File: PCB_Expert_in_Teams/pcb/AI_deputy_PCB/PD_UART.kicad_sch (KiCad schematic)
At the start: 1 part, among them J2 Battery Input

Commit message: updating repo from desktop
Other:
- company: (none) -> Area 42 & Albers-Online Psykologi
- title: (none) -> AI Deputy
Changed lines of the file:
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@@
 	(generator_version "9.0")
 	(paper "A4")
+	(title_block
+		(title "AI Deputy")
+		(date "2025-09-24")
+		(rev "v0.1")
+		(company "Area 42 & Albers-Online Psykologi")
+		(comment 1 "SDU")
+		(comment 2 "Expert In Teams Semester Project")
+	)
 	(text_box "Battery input from BMS\n"
 		(exclude_from_sim no)

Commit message: 29/10/update
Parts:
- removed J2: Battery Input, symbol Connector:Conn_01x02_Pin
- added C38, C41, C45, C47, C48: 4u7, symbol Device:C
- added C39, C40, C42, C49: 100n, symbol Device:C
- added D3: LED, LED_SMD:LED_0805_2012Metric_Pad1.15x1.40mm_HandSolder, symbol Device:LED
- added IC7: CYPD3177-24LQXQ, QFN50P400X400X60-25N-D, symbol CYPD3177-24LQXQ:CYPD3177-24LQXQ
- added J16: USB_C_Receptacle_USB2.0_16P, EXT_AI_DEPUTY_Library:MOLEX_1054500101, symbol Connector:USB_C_Receptacle_USB2.0_16P
- added Q2, Q4: DMP3098LSD-13, SOIC127P600X175-8N, symbol DMP3098LSD:DMP3098LSD-13
- added R20, R22, R24: 5.1k, Resistor_SMD:R_0805_2012Metric_Pad1.20x1.40mm_HandSolder, symbol Device:R
- added R21, R25, R35: 1k, Resistor_SMD:R_0805_2012Metric_Pad1.20x1.40mm_HandSolder, symbol Device:R
- added R23: 2.4k, Resistor_SMD:R_0805_2012Metric_Pad1.20x1.40mm_HandSolder, symbol Device:R
- added R26: 2.2k, Resistor_SMD:R_0805_2012Metric_Pad1.20x1.40mm_HandSolder, symbol Device:R
- added R27, R28, R29, R31, R32: 2k2, symbol Device:R
- added R30: 20k, symbol Device:R
- added R33: 10k, Resistor_SMD:R_0805_2012Metric_Pad1.20x1.40mm_HandSolder, symbol Device:R
- added R34: 4.7k, Resistor_SMD:R_0805_2012Metric_Pad1.20x1.40mm_HandSolder, symbol Device:R
- added R36: 50k, Resistor_SMD:R_0805_2012Metric_Pad1.20x1.40mm_HandSolder, symbol Device:R
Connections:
- net GND: now also C38.2, C39.2, C40.2, C41.2, C42.2, C45.2, C48.2, D3.1 (K), IC7.19 (GND_1), IC7.22 (GND_2), IC7.25 (GND_3), J16.A1 (GND), J16.A12 (GND), J16.B1 (GND), J16.B12 (GND), R21.2, R23.2, R25.2, R26.2
- new net: C45.1, IC7.24 (VCCD)
- new net: C47.2, C49.2, R30.2, R31.2, R32.1
- new net: IC7.10 (FLIP), R34.2
- new net: IC7.1 (VBUS_MIN), R20.2, R21.1
- new net: IC7.5 (ISNK_COARSE), R22.2, R23.1
- new net: D3.2 (A), R33.2
- new net: Q4.1 (S1), Q4.3 (S2)
- new net: Q4.2 (G1), Q4.4 (G2), R31.1
- new net: IC7.2 (VBUS_MAX), R24.2, R25.1
- new net: IC7.6 (ISNK_FINE), R26.1
- new net: Q2.1 (S1), Q2.3 (S2)
- new net: Q2.2 (G1), Q2.4 (G2), R35.1, R36.2
- new net +3V3: C38.1, C39.1, C40.1, IC7.23 (VDDD), R20.1, R22.1, R24.1, R27.1, R28.1, R29.1, R34.1
- new net CC1: IC7.15 (CC1), J16.A5 (CC1)
- new net CC2: IC7.14 (CC2), J16.B5 (CC2)
- new net D+: J16.A6 (D+), J16.B6 (D+)
- new net D-: J16.A7 (D-), J16.B7 (D-)
- new net PD_Fault: IC7.9 (FAULT), R33.1
- new net PD_INT: IC7.7 (HPI_INT), R29.2
- new net SAFE_PWR_EN: IC7.4 (SAFE_PWR_EN), R35.2
- new net SCL: IC7.13 (HPI_SCL), R27.2
- new net SDA: IC7.12 (HPI_SDA), R28.2
- new net VBUS: C41.1, C42.1, C47.1, IC7.18 (VBUS_IN), J16.A4 (VBUS), J16.A9 (VBUS), J16.B4 (VBUS), J16.B9 (VBUS), Q2.7 (D1_1), Q2.8 (D1_2), Q4.7 (D1_1), Q4.8 (D1_2), R30.1, R36.1
- new net VBUSEN: IC7.3 (VBUS_FET_EN), R32.2
- new net VDC_OUT: C48.1, C49.1, IC7.11 (VDC_OUT), Q4.6 (D2_2)
- new net VIN: Q2.5 (D2_1), Q2.6 (D2_2)
- no-connect marks 0 -> 8
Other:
- note added: "1/6 for 9V (see datasheet for config)"
- note added: "Fuse or TVS?"
- note added: "USB-C 3.0 footprint?"
- note added: "VIN goes to input 3v3 step down converter"
- note added: "current config is 2A, 5.1k up and 5.1k down for 3A"
- note added: "find fitting res value for led"

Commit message: update some schematic footprints
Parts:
- IC7: footprint QFN50P400X400X60-25N-D -> EXT_AI_DEPUTY_Library:QFN50P400X400X60-25N-D
- Q2, Q4: footprint SOIC127P600X175-8N -> EXT_AI_DEPUTY_Library:SOIC127P600X175-8N
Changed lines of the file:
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@@
 			)
 		)
-		(property "Footprint" "SOIC127P600X175-8N"
+		(property "Footprint" "EXT_AI_DEPUTY_Library:SOIC127P600X175-8N"
 			(at 223.52 -51.74 0)
 			(effects
@@
 			)
 		)
-		(property "Footprint" "QFN50P400X400X60-25N-D"
+		(property "Footprint" "EXT_AI_DEPUTY_Library:QFN50P400X400X60-25N-D"
 			(at 168.91 154.61 0)
 			(effects
@@
 			)
 		)
-		(property "Footprint" "SOIC127P600X175-8N"
+		(property "Footprint" "EXT_AI_DEPUTY_Library:SOIC127P600X175-8N"
 			(at 222.25 42.24 0)
 			(effects

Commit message: update pcb from desktop
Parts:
- C38, C39, C40, C41, C42, C45, C48, C49: footprint (none) -> Capacitor_SMD:C_0805_2012Metric_Pad1.18x1.45mm_HandSolder
- R27, R28, R29, R30, R31, R32: footprint (none) -> Resistor_SMD:R_0805_2012Metric_Pad1.20x1.40mm_HandSolder
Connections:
- net VDC_OUT: now also Q4.5 (D2_1)
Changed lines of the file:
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@@
 	)
 	(junction
+		(at 215.9 35.56)
+		(diameter 0)
+		(color 0 0 0 0)
+	)
+	(junction
 		(at 68.58 81.28)
 		(diameter 0)
@@
 	(wire
 		(pts
+			(xy 215.9 35.56) (xy 219.71 35.56)
+		)
+		(stroke
+			(width 0)
+			(type default)
+		)
+	)
+	(wire
+		(pts
 			(xy 207.01 63.5) (xy 251.46 63.5)
 		)
@@
 	(wire
 		(pts
+			(xy 215.9 35.56) (xy 215.9 17.78)
+		)
+		(stroke
+			(width 0)
+			(type default)
+		)
+	)
+	(wire
+		(pts
 			(xy 215.9 153.67) (xy 219.71 153.67)
 		)
@@
 	(wire
 		(pts
-			(xy 215.9 38.1) (xy 215.9 17.78)
+			(xy 215.9 38.1) (xy 215.9 35.56)
 		)
 		(stroke
@@
 			)
 		)
-		(property "Footprint" ""
+		(property "Footprint" "Resistor_SMD:R_0805_2012Metric_Pad1.20x1.40mm_HandSolder"
 			(at 187.452 96.52 90)
 			(effects
@@
 			)
 		)
-		(property "Footprint" ""
+		(property "Footprint" "Capacitor_SMD:C_0805_2012Metric_Pad1.18x1.45mm_HandSolder"
 			(at 127.9652 40.64 0)
 			(effects
@@
 			)
 		)
-		(property "Footprint" ""
+		(property "Footprint" "Capacitor_SMD:C_0805_2012Metric_Pad1.18x1.45mm_HandSolder"
 			(at 134.3152 50.8 0)
 			(effects
@@
 			)
 		)
-		(property "Footprint" ""
+		(property "Footprint" "Capacitor_SMD:C_0805_2012Metric_Pad1.18x1.45mm_HandSolder"
 			(at 72.0852 57.15 0)
 			(effects
@@
 			)
 		)
-		(property "Footprint" ""
+		(property "Footprint" "Capacitor_SMD:C_0805_2012Metric_Pad1.18x1.45mm_HandSolder"
 			(at 83.5152 57.15 0)
 			(effects
@@
 			)
 		)
-		(property "Footprint" ""
+		(property "Footprint" "Resistor_SMD:R_0805_2012Metric_Pad1.20x1.40mm_HandSolder"
 			(at 205.232 54.61 90)
 			(effects
@@
 			)
 		)
-		(property "Footprint" ""
+		(property "Footprint" "Resistor_SMD:R_0805_2012Metric_Pad1.20x1.40mm_HandSolder"
 			(at 249.682 69.85 90)
 			(effects
@@
 			)
 		)
-		(property "Footprint" ""
+		(property "Footprint" "Capacitor_SMD:C_0805_2012Metric_Pad1.18x1.45mm_HandSolder"
 			(at 103.8352 40.64 0)
 			(effects
@@
 			)
 		)
-		(property "Footprint" ""
+		(property "Footprint" "Capacitor_SMD:C_0805_2012Metric_Pad1.18x1.45mm_HandSolder"
 			(at 239.7252 25.4 0)
 			(effects
@@
 			)
 		)
-		(property "Footprint" ""
+		(property "Footprint" "Resistor_SMD:R_0805_2012Metric_Pad1.20x1.40mm_HandSolder"
 			(at 179.832 96.52 90)
 			(effects
@@
 			)
 		)
-		(property "Footprint" ""
+		(property "Footprint" "Capacitor_SMD:C_0805_2012Metric_Pad1.18x1.45mm_HandSolder"
 			(at 115.2652 40.64 0)
 			(effects
@@
 			)
 		)
-		(property "Footprint" ""
+		(property "Footprint" "Capacitor_SMD:C_0805_2012Metric_Pad1.18x1.45mm_HandSolder"
 			(at 229.5652 25.4 0)
 			(effects
@@
 			)
 		)
-		(property "Footprint" ""
+		(property "Footprint" "Resistor_SMD:R_0805_2012Metric_Pad1.20x1.40mm_HandSolder"
 			(at 195.072 96.52 90)
 			(effects
@@
 			)
 		)
-		(property "Footprint" ""
+		(property "Footprint" "Resistor_SMD:R_0805_2012Metric_Pad1.20x1.40mm_HandSolder"
 			(at 249.682 55.88 90)
 			(effects

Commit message: update schematic from desktop
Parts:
- removed C41: 4u7, Capacitor_SMD:C_0805_2012Metric_Pad1.18x1.45mm_HandSolder, symbol Device:C
- removed C42: 100n, Capacitor_SMD:C_0805_2012Metric_Pad1.18x1.45mm_HandSolder, symbol Device:C
- removed J16: USB_C_Receptacle_USB2.0_16P, EXT_AI_DEPUTY_Library:MOLEX_1054500101, symbol Connector:USB_C_Receptacle_USB2.0_16P
- added C50: 4u7, Capacitor_SMD:C_0805_2012Metric_Pad1.18x1.45mm_HandSolder, symbol Device:C
- added C51: 100n, Capacitor_SMD:C_0805_2012Metric_Pad1.18x1.45mm_HandSolder, symbol Device:C
- added J16, J17: Conn_01x01_Pin, TestPoint:TestPoint_Pad_4.0x4.0mm, symbol Connector:Conn_01x01_Pin
- added J2: 2171790001, EXT_AI_DEPUTY_Library:MOLEX_2171790001, symbol USBC-2.0-16p-molex-217179:2171790001
- C47: footprint (none) -> Capacitor_SMD:C_0805_2012Metric_Pad1.18x1.45mm_HandSolder
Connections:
- net CC1: now also J2.A5 (CC1)
- net CC2: now also J2.B5 (CC2)
- net D+: now also J2.A6 (DP1), J2.B6 (DP2)
- net D-: now also J2.A7 (DN1), J2.B7 (DN2)
- net GND: now also C50.2, C51.2, J17.1 (Pin_1), J2.A1B12 (GND1), J2.B1A12 (GND2)
- net SAFE_PWR_EN: now also R35.1; no longer R35.2
- net VBUS: now also C50.1, C51.1, J2.A4B9 (VBUS1), J2.B4A9 (VBUS2)
- net VDC_OUT: now also J16.1 (Pin_1)
- net at Q2.2 (G1), Q2.4 (G2), R36.2: now also R35.2; no longer R35.1
- no-connect marks 8 -> 11
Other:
- note added: "USB-C 2.0 16p"
- note added: "battery gnd"
- note added: "pd output voltage 9V"
- note removed: "Fuse or TVS?"
- note removed: "USB-C 3.0 footprint?"
- moved on the sheet: R35

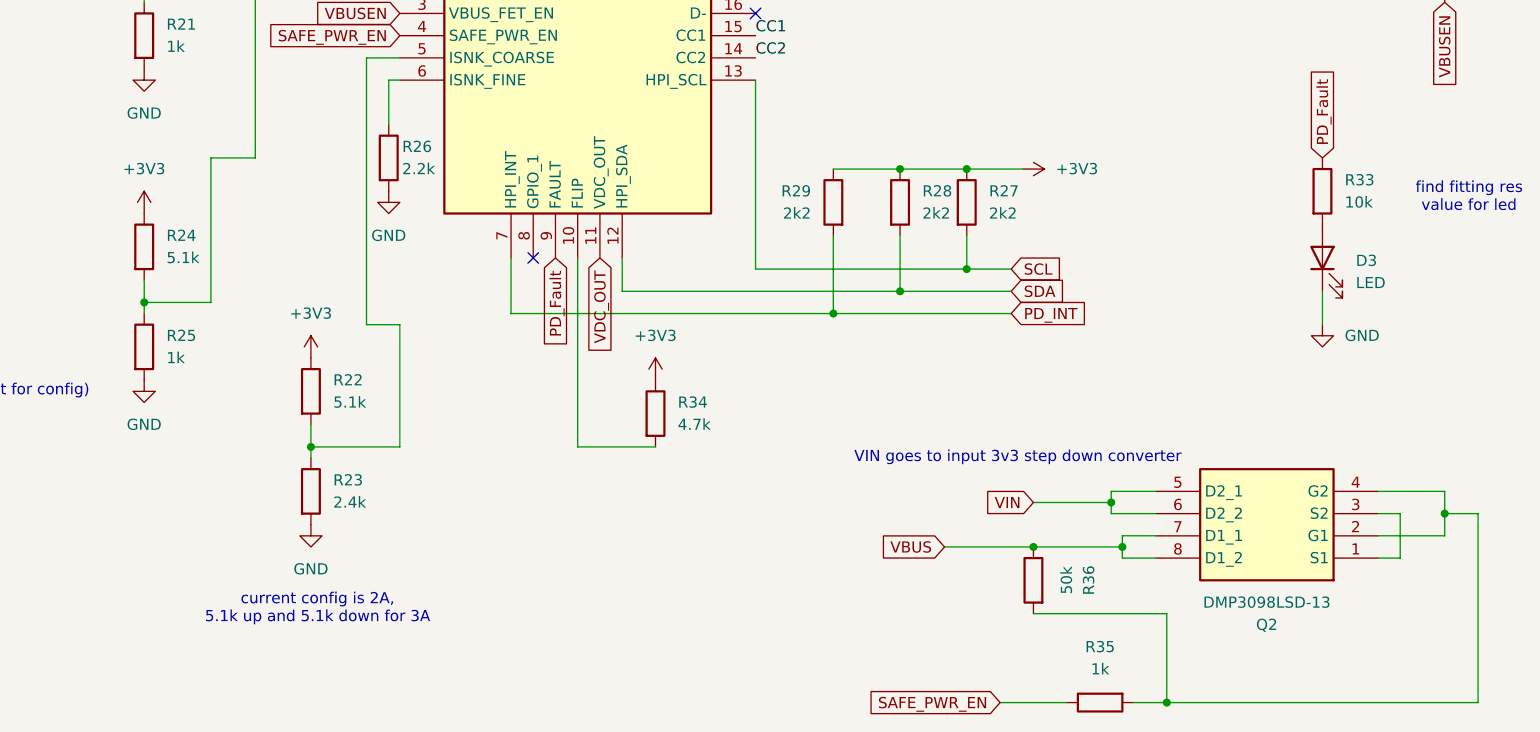
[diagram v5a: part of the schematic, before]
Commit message: pcb updates from desktop with schematic fix
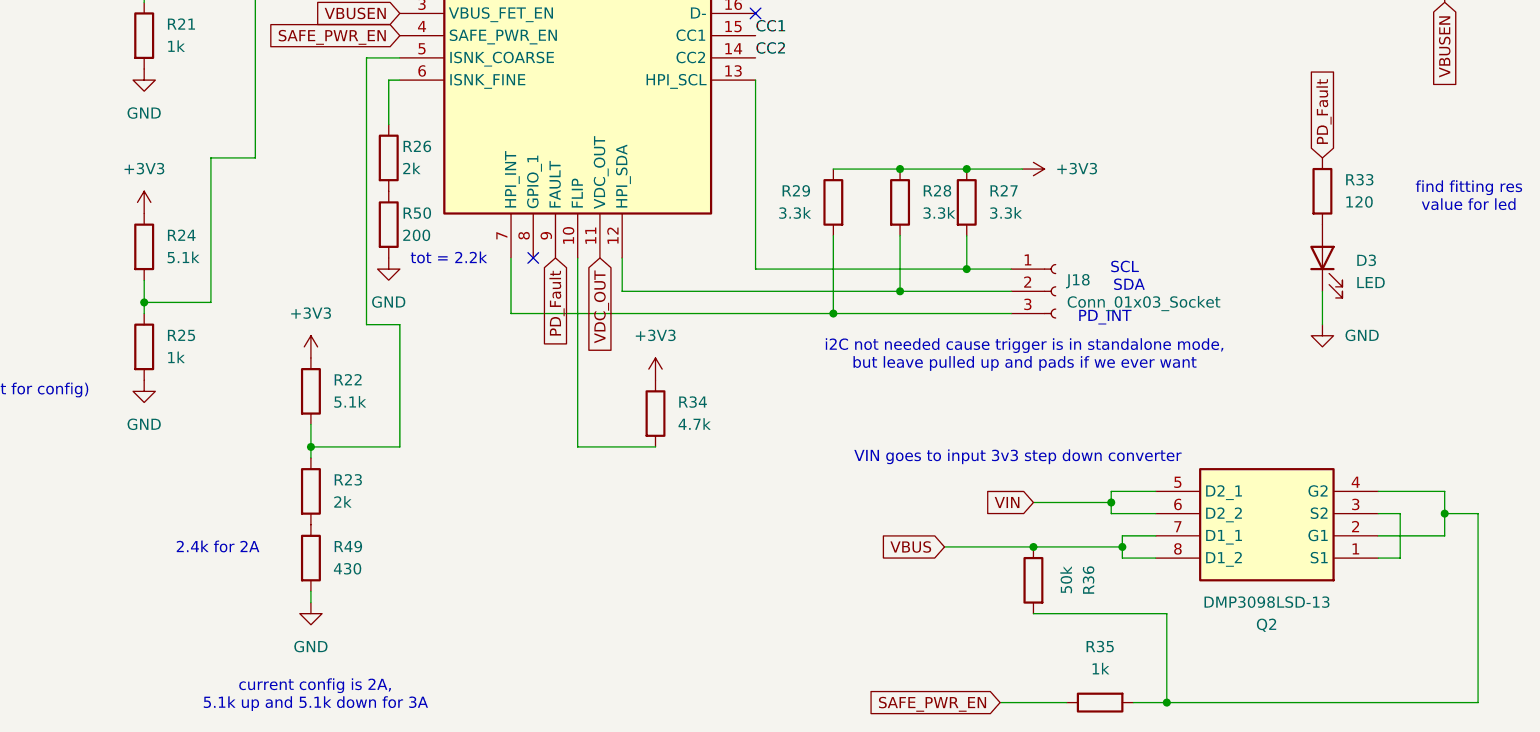
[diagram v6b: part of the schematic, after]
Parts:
- added J18: Conn_01x03_Socket, Connector_PinHeader_2.54mm:PinHeader_1x03_P2.54mm_Vertical, symbol Connector:Conn_01x03_Socket
- added R49: 430, Resistor_SMD:R_0805_2012Metric_Pad1.20x1.40mm_HandSolder, symbol Device:R
- added R50: 200, Resistor_SMD:R_0805_2012Metric_Pad1.20x1.40mm_HandSolder, symbol Device:R
- R23: value 2.4k -> 2k
- R26: value 2.2k -> 2k
- R27, R28, R29: value 2k2 -> 3.3k
- R33: value 10k -> 120
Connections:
- net GND: now also R49.2, R50.2; no longer R23.2, R26.2
- net PD_INT: no longer names the net of IC7.7 (HPI_INT), R29.2
- net PD_INT: now also J18.3 (Pin_3)
- net SCL: no longer names the net of IC7.13 (HPI_SCL), R27.2
- net SCL: now also J18.1 (Pin_1)
- net SDA: no longer names the net of IC7.12 (HPI_SDA), R28.2
- net SDA: now also J18.2 (Pin_2)
- new net: R23.2, R49.1
- new net: R26.2, R50.1
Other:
- note added: "2.4k for 2A"
- note added: "PD_INT"
- note added: "SCL"
- note added: "SDA"
- note added: "i2C not needed cause trigger is in standalone mode, but leave pulled up and pads if we ever want"
- note added: "tot = 2.2k"

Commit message: before saturday work
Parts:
- R34: value 4.7k -> 51k
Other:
- note added: "Changed from 4.7k to 51k to turn off data capability"
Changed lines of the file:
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@@
+		)
+	)
+	(text "Changed from 4.7k to 51k \nto turn off data capability"
+		(exclude_from_sim no)
+		(at 156.21 128.778 0)
+		(effects
+			(font
+				(size 1.27 1.27)
+			)
 		)
 	)
@@
 			)
 		)
-		(property "Value" "4.7k"
+		(property "Value" "51k"
 			(at 163.83 121.9199 0)
 			(effects

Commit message: updated pcb code
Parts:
- R36: value 50k -> 51k
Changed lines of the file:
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@@
 			)
 		)
-		(property "Value" "50k"
+		(property "Value" "51k"
 			(at 208.28 139.7 90)
 			(effects
